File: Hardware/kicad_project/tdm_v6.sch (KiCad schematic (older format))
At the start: 39 parts, among them J1 picoprobe_debug, J2 USB_C_Receptacle_USB2.0, SW26 spst_4_pin_internal, SW27 spst_4_pin_internal, U1 W25Q32JVSS, U2 RP2040, Y1 Crystal_GND24

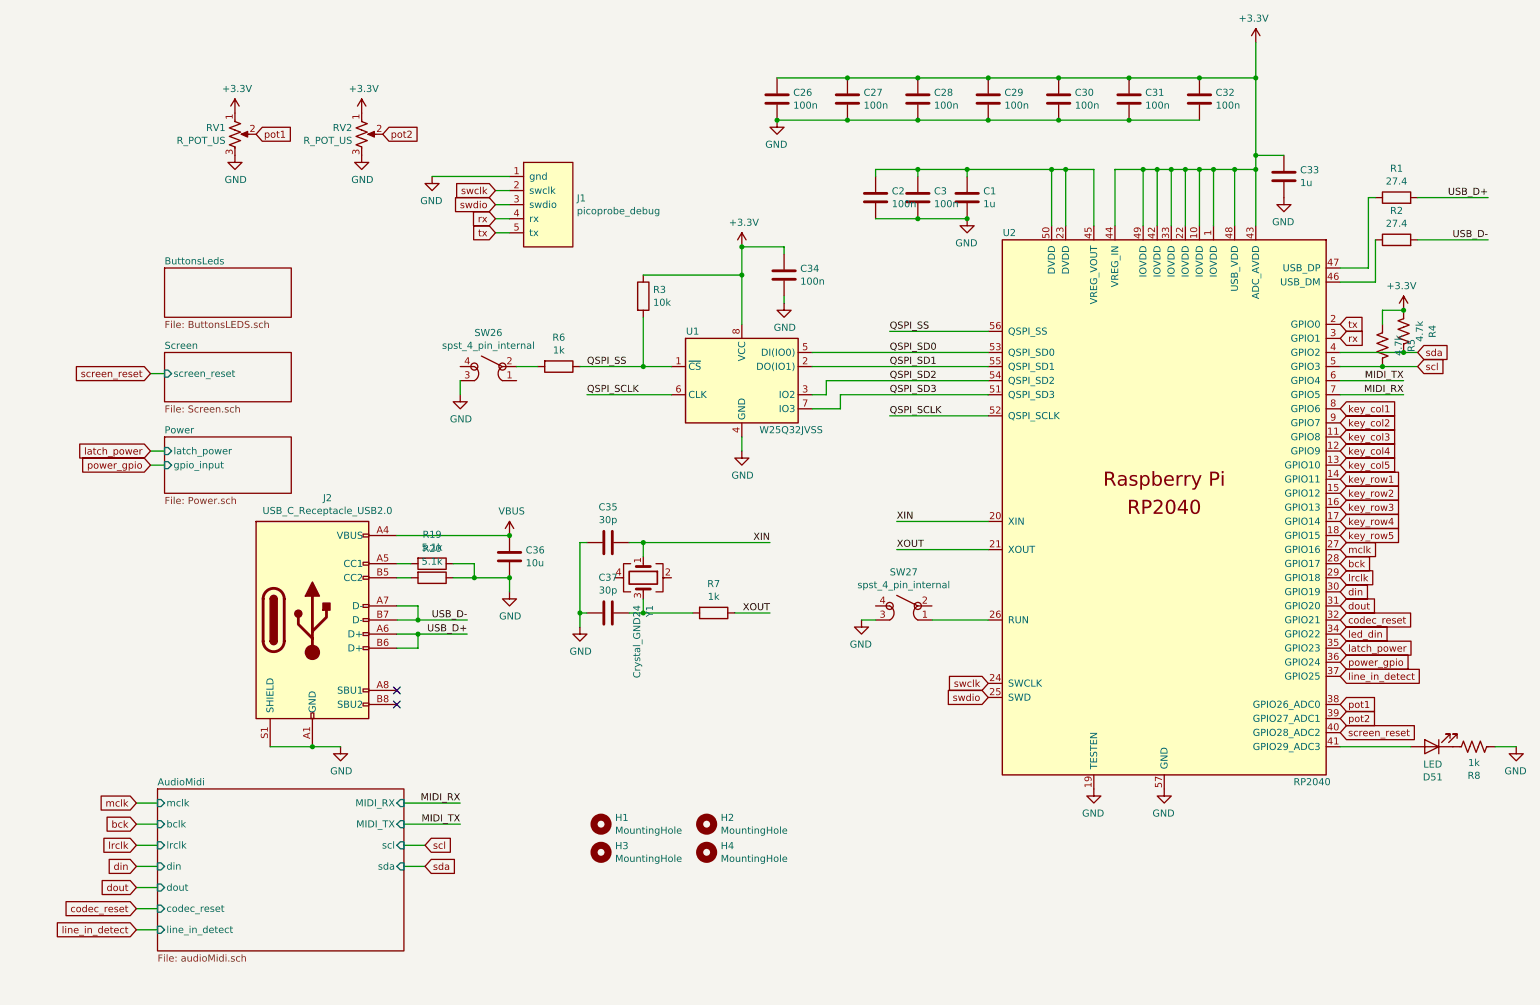
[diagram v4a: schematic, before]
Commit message: new hardware rev
reworked power system
added amp
new LDOS (less dropout)
dedicated LDO for audio system
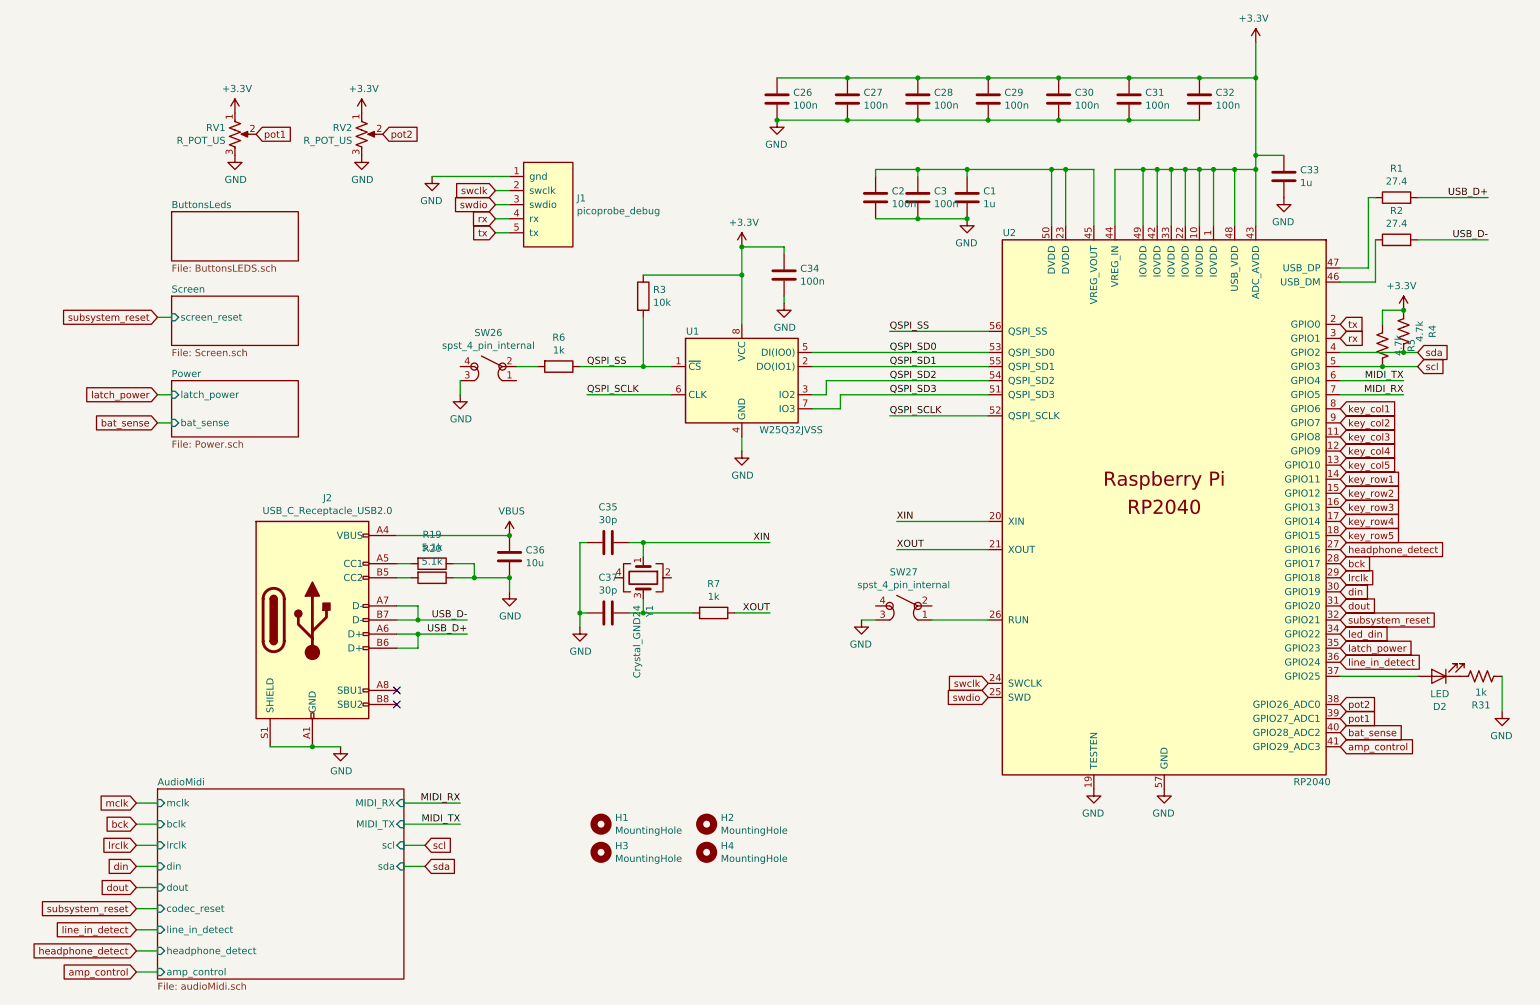
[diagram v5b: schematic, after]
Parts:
- removed D51: LED, LEDs:LED_0603, symbol Device:LED
- removed R8: 1k, Resistors_SMD:R_0402_NoSilk, symbol Device:R_US
- added D2: LED, LEDs:LED_0603, symbol Device:LED
- added R31: 1k, Resistors_SMD:R_0402_NoSilk, symbol Device:R_US
- Y1: checked (none) -> 1
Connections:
- net power_gpio is gone; now on net line_in_detect: U2.36 (GPIO24)
- net GND: now also R31.2
- net line_in_detect: no longer U2.37 (GPIO25)
- net mclk: no longer U2.27 (GPIO16)
- net pot1: now also U2.39 (GPIO27_ADC1); no longer U2.38 (GPIO26_ADC0)
- net pot2: now also U2.38 (GPIO26_ADC0); no longer U2.39 (GPIO27_ADC1)
- net amp_control: now reaches U2.41 (GPIO29_ADC3)
- net codec_reset renamed subsystem_reset
- net screen_reset renamed bat_sense
- new net: D2.2 (A), U2.37 (GPIO25)
- new net: D2.1 (K), R31.1
- new net headphone_detect: U2.27 (GPIO16)
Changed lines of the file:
@@
 	1    0    0    -1
 $EndComp
+Text GLabel 9850 5700 2    50   Input ~ 0
+pot1
 Text GLabel 9850 5600 2    50   Input ~ 0
-pot1
-Text GLabel 9850 5700 2    50   Input ~ 0
 pot2
-Text GLabel 9850 5100 2    50   Input ~ 0
-led_din
 Text GLabel 9850 3500 2    50   Input ~ 0
 key_col1
@@
 Wire Wire Line
 	10400 2300 10900 2300
-Text GLabel 9850 4500 2    50   Input ~ 0
-mclk
-Text GLabel 9850 4600 2    50   Input ~ 0
-bck
-Text GLabel 9850 5000 2    50   Input ~ 0
-codec_reset
-Text GLabel 9850 4900 2    50   Input ~ 0
-dout
-Text GLabel 9850 4800 2    50   Input ~ 0
-din
-Text GLabel 9850 4700 2    50   Input ~ 0
-lrclk
 $Comp
 L Memory_Flash:W25Q32JVSS U1
@@
 Wire Wire Line
 	9850 3400 10300 3400
-$Comp
-L Device:LED D51
-U 1 1 61FD1144
-P 10500 5900
-F 0 "D51" H 10493 6116 50  0000 C CNN
-F 1 "LED" H 10493 6025 50  0000 C CNN
-F 2 "LEDs:LED_0603" H 10500 5900 50  0001 C CNN
-F 3 "~" H 10500 5900 50  0001 C CNN
-F 4 "c2286" H 10500 5900 50  0001 C CNN "LCSC"
-	1    10500 5900
-	-1   0    0    1
-$EndComp
-$Comp
-L Device:R_US R8
-U 1 1 61FD114B
-P 10800 5900
-F 0 "R8" V 10595 5900 50  0000 C CNN
-F 1 "1k" V 10686 5900 50  0000 C CNN
-F 2 "Resistors_SMD:R_0402_NoSilk" V 10840 5890 50  0001 C CNN
-F 3 "~" H 10800 5900 50  0001 C CNN
-F 4 "C11702" H 10800 5900 50  0001 C CNN "LCSC"
-	1    10800 5900
-	0    -1   -1   0
-$EndComp
-$Comp
-L power:GND #PWR019
-U 1 1 6204155A
-P 11100 5900
-F 0 "#PWR019" H 11100 5650 50  0001 C CNN
-F 1 "GND" H 11105 5727 50  0000 C CNN
-F 2 "" H 11100 5900 50  0001 C CNN
-F 3 "" H 11100 5900 50  0001 C CNN
-	1    11100 5900
-	-1   0    0    -1
-$EndComp
-Wire Wire Line
-	10950 5900 11100 5900
 Wire Wire Line
 	9250 900  9250 1150
@@
 	3200 6450 3600 6450
 $Sheet
-S 1450 6200 1750 1150
+S 1450 6200 1750 1350
 U 62E6C628
 F0 "AudioMidi" 50
@@
 F11 "sda" I R 3200 6750 50
 F12 "line_in_detect" I L 1450 7200 50
+F13 "headphone_detect" I L 1450 7350 50
+F14 "amp_control" I L 1450 7500 50
 $EndSheet
 $Sheet
-S 1500 2500 900  350
+S 1550 2100 900  350
 U 631EE57A
 F0 "ButtonsLeds" 50
@@
 Text GLabel 1300 6450 0    50   Input ~ 0
 bck
-Text GLabel 1300 7050 0    50   Input ~ 0
-codec_reset
 Text GLabel 1300 6900 0    50   Input ~ 0
 dout
@@
 	1300 7050 1450 7050
 $Sheet
-S 1500 3100 900  350
+S 1550 2700 900  350
 U 63637E58
 F0 "Screen" 50
 F1 "Screen.sch" 50
-F2 "screen_reset" I L 1500 3250 50
+F2 "screen_reset" I L 1550 2850 50
 $EndSheet
 $Sheet
-S 1500 3700 900  400
+S 1550 3300 900  400
 U 6366865E
 F0 "Power" 50
 F1 "Power.sch" 50
-F2 "latch_power" I L 1500 3800 50
-F3 "gpio_input" I L 1500 3900 50
+F2 "latch_power" I L 1550 3400 50
+F3 "bat_sense" I L 1550 3600 50
 $EndSheet
 $Comp
@@
 F 3 "~" H 4900 4700 50  0001 C CNN
 F 4 "C97242" H 4900 4700 50  0001 C CNN "LCSC"
+F 5 "1" H 4900 4700 50  0001 C CNN "checked"
 	1    4900 4700
 	0    1    1    0
@@
 Wire Wire Line
 	6850 2150 7200 2150
-Text GLabel 1400 3800 0    50   Input ~ 0
+Text GLabel 1450 3400 0    50   Input ~ 0
 latch_power
-Text GLabel 1400 3900 0    50   Input ~ 0
-power_gpio
-Text GLabel 1400 3250 0    50   Input ~ 0
-screen_reset
-Text GLabel 9850 5300 2    50   Input ~ 0
-power_gpio
-Text GLabel 9850 5800 2    50   Input ~ 0
-screen_reset
-Wire Wire Line
-	1400 3250 1500 3250
-Wire Wire Line
-	1400 3800 1500 3800
-Wire Wire Line
-	1400 3900 1500 3900
+Wire Wire Line
+	1450 2850 1550 2850
+Wire Wire Line
+	1450 3400 1550 3400
 Text GLabel 1300 7200 0    50   Input ~ 0
 line_in_detect
 Wire Wire Line
 	1300 7200 1450 7200
-Text GLabel 9850 5400 2    50   Input ~ 0
-line_in_detect
+Text GLabel 1450 2850 0    50   Input ~ 0
+subsystem_reset
+Text GLabel 1300 7050 0    50   Input ~ 0
+subsystem_reset
+Text GLabel 9850 4500 2    50   Input ~ 0
+headphone_detect
+Text GLabel 1300 7350 0    50   Input ~ 0
+headphone_detect
+Wire Wire Line
+	1300 7350 1450 7350
 Text GLabel 9850 5200 2    50   Input ~ 0
 latch_power
-Wire Wire Line
-	9850 5900 10350 5900
+Text GLabel 9850 4700 2    50   Input ~ 0
+lrclk
+Text GLabel 9850 4800 2    50   Input ~ 0
+din
+Text GLabel 9850 4900 2    50   Input ~ 0
+dout
+Text GLabel 9850 5000 2    50   Input ~ 0
+subsystem_reset
+Text GLabel 9850 4600 2    50   Input ~ 0
+bck
+Text GLabel 9850 5100 2    50   Input ~ 0
+led_din
+Text GLabel 9850 5300 2    50   Input ~ 0
+line_in_detect
+Text GLabel 1450 3600 0    50   Input ~ 0
+bat_sense
+Wire Wire Line
+	1450 3600 1550 3600
+Text GLabel 9850 5800 2    50   Input ~ 0
+bat_sense
+Text GLabel 9850 5900 2    50   Input ~ 0
+amp_control
+Text GLabel 1300 7500 0    50   Input ~ 0
+amp_control
+Wire Wire Line
+	1300 7500 1450 7500
+$Comp
+L Device:LED D?
+U 1 1 6262BF3C
+P 10550 5400
+AR Path="/6366865E/6262BF3C" Ref="D?"  Part="1"
+AR Path="/6262BF3C" Ref="D2"  Part="1"
+F 0 "D2" H 10543 5616 50  0000 C CNN
+F 1 "LED" H 10543 5525 50  0000 C CNN
+F 2 "LEDs:LED_0603" H 10550 5400 50  0001 C CNN
+F 3 "~" H 10550 5400 50  0001 C CNN
+F 4 "c2286" H 10550 5400 50  0001 C CNN "LCSC"
+	1    10550 5400
+	-1   0    0    1
+$EndComp
+$Comp
+L Device:R_US R?
+U 1 1 6262BF43
+P 10850 5400
+AR Path="/6366865E/6262BF43" Ref="R?"  Part="1"
+AR Path="/6262BF43" Ref="R31"  Part="1"
+F 0 "R31" V 10645 5400 50  0000 C CNN
+F 1 "1k" V 10736 5400 50  0000 C CNN
+F 2 "Resistors_SMD:R_0402_NoSilk" V 10890 5390 50  0001 C CNN
+F 3 "~" H 10850 5400 50  0001 C CNN
+F 4 "C11702" H 10850 5400 50  0001 C CNN "LCSC"
+	1    10850 5400
+	0    -1   -1   0
+$EndComp
+$Comp
+L power:GND #PWR0128
+U 1 1 62633279
+P 11000 5650
+F 0 "#PWR0128" H 11000 5400 50  0001 C CNN
+F 1 "GND" H 11005 5477 50  0000 C CNN
+F 2 "" H 11000 5650 50  0001 C CNN
+F 3 "" H 11000 5650 50  0001 C CNN
+	1    11000 5650
+	-1   0    0    -1
+$EndComp
+Wire Wire Line
+	9850 5400 10400 5400
+Wire Wire Line
+	11000 5400 11000 5650
 $EndSCHEMATC
